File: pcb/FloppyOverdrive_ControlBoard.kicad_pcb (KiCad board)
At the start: 2 copper layers, 163 x 104 mm, 0 parts

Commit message: PCB Update
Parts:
- added C1: 0.1u, Capacitor_THT:C_Disc_D5.0mm_W2.5mm_P2.50mm, F.Cu at (206.0, 97.0)
- added C2: 0.1u, Capacitor_THT:C_Disc_D5.0mm_W2.5mm_P2.50mm, F.Cu at (211.0, 97.0)
- added C3: 33u, Capacitor_THT:CP_Radial_D5.0mm_P2.00mm, F.Cu at (208.5, 65.0)
- added C4: 33u, Capacitor_THT:CP_Radial_D5.0mm_P2.00mm, F.Cu at (208.4, 57.0)
- added C5: 0.1u, Capacitor_THT:C_Disc_D5.0mm_W2.5mm_P2.50mm, F.Cu at (206.0, 91.0)
- added C6: 0.1u, Capacitor_THT:C_Disc_D5.0mm_W2.5mm_P2.50mm, F.Cu at (211.0, 91.0)
- added C7: 0.1u, Capacitor_THT:C_Disc_D5.0mm_W2.5mm_P2.50mm, F.Cu at (121.1, 42.0)
- added D1: LED1, LED_THT:LED_D5.0mm, F.Cu at (170.0, 98.0)
- added D2: LED2, LED_THT:LED_D5.0mm, F.Cu at (177.0, 98.0)
- added D3: LED3, LED_THT:LED_D5.0mm, F.Cu at (184.0, 98.0)
- added D4: LED4, LED_THT:LED_D5.0mm, F.Cu at (191.0, 98.0)
- added FB1: FerriteBead, Resistor_SMD:R_1206_3216Metric, F.Cu at (209.0, 71.0)
- added FB2: FerriteBead, Resistor_SMD:R_1206_3216Metric, F.Cu at (209.0, 50.3)
- added J1: 174804-1, 174804-1:1748041, F.Cu at (216.2, 53.4)
- added J2: Motor_Header, 440055-4:SHDRRA4W50P15X200_1X4_1000X770X525P, F.Cu at (194.2, 134.4)
- added J3: Bus_Connector, Connector_PinHeader_2.54mm:PinHeader_2x17_P2.54mm_Horizontal, F.Cu at (212.0, 102.0)
- added J4: Sensor_Header, Connector_PinHeader_2.54mm:PinHeader_2x05_P2.54mm_Horizontal, F.Cu at (78.7, 142.1)
- added J5: Heads_Header, Connector_PinHeader_2.54mm:PinHeader_2x05_P2.54mm_Horizontal, F.Cu at (78.7, 114.1)
- added J6: Step_Header, Connector_PinHeader_2.00mm:PinHeader_2x05_P2.00mm_Horizontal, F.Cu at (187.0, 134.9)
- added J7: PIC_ADC_Header, Connector_PinHeader_2.54mm:PinHeader_2x02_P2.54mm_Vertical, F.Cu at (144.0, 23.4)
- added J8: FPGA_IO_Header, Connector_PinHeader_2.54mm:PinHeader_2x20_P2.54mm_Vertical, F.Cu at (115.0, 143.0)
- added J9: HeadOut_Header, Connector_PinHeader_2.54mm:PinHeader_2x04_P2.54mm_Vertical, F.Cu at (93.3, 112.8)
- added JP1: LED_Enable, Connector_PinHeader_2.54mm:PinHeader_1x02_P2.54mm_Vertical, F.Cu at (199.0, 97.0)
- added R1: 220, Resistor_THT:R_Axial_DIN0207_L6.3mm_D2.5mm_P10.16mm_Horizontal, F.Cu at (48.9, 82.0)
- added R10: 47k, Resistor_THT:R_Axial_DIN0207_L6.3mm_D2.5mm_P10.16mm_Horizontal, F.Cu at (59.8, 66.4)
- added R11: 1k, Resistor_THT:R_Axial_DIN0207_L6.3mm_D2.5mm_P10.16mm_Horizontal, F.Cu at (72.0, 62.3)
- added R12: 510, Resistor_THT:R_Axial_DIN0207_L6.3mm_D2.5mm_P10.16mm_Horizontal, F.Cu at (164.1, 95.0)
- added R13: 510, Resistor_THT:R_Axial_DIN0207_L6.3mm_D2.5mm_P10.16mm_Horizontal, F.Cu at (153.9, 98.0)
- added R14: 510, Resistor_THT:R_Axial_DIN0207_L6.3mm_D2.5mm_P10.16mm_Horizontal, F.Cu at (164.1, 101.0)
- added R15: 510, Resistor_THT:R_Axial_DIN0207_L6.3mm_D2.5mm_P10.16mm_Horizontal, F.Cu at (164.1, 104.0)
- added R2: 220, Resistor_THT:R_Axial_DIN0207_L6.3mm_D2.5mm_P10.16mm_Horizontal, F.Cu at (35.5, 82.0)
- added R3: 220, Resistor_THT:R_Axial_DIN0207_L6.3mm_D2.5mm_P10.16mm_Horizontal, F.Cu at (62.2, 82.6)
- added R4: 47k, Resistor_THT:R_Axial_DIN0207_L6.3mm_D2.5mm_P10.16mm_Horizontal, F.Cu at (59.8, 70.4)
- added R5: 10k, Resistor_THT:R_Axial_DIN0207_L6.3mm_D2.5mm_P10.16mm_Horizontal, F.Cu at (115.5, 37.9)
- added R6: 1k, Resistor_THT:R_Axial_DIN0207_L6.3mm_D2.5mm_P10.16mm_Horizontal, F.Cu at (73.1, 66.4)
- added R7: 1k, Resistor_THT:R_Axial_DIN0207_L6.3mm_D2.5mm_P10.16mm_Horizontal, F.Cu at (58.7, 62.3)
- added R8: 22k, Resistor_THT:R_Axial_DIN0207_L6.3mm_D2.5mm_P10.16mm_Horizontal, F.Cu at (73.1, 70.4)
- added R9: 220, Resistor_THT:R_Axial_DIN0207_L6.3mm_D2.5mm_P10.16mm_Horizontal, F.Cu at (62.2, 78.5)
- added SW1: RST_Btn, Button_Switch_THT:SW_PUSH_6mm, F.Cu at (138.2, 103.2)
- added U1: TXB0108-PW, Package_SO:TSSOP-20_4.4x6.5mm_P0.65mm, F.Cu at (197.0, 112.0)
- added U2: TXB0108-PW, Package_SO:TSSOP-20_4.4x6.5mm_P0.65mm, F.Cu at (197.0, 122.0)
- added U3: ULN2003, Package_SO:TSSOP-16_4.4x5mm_P0.65mm, F.Cu at (184.0, 128.0)
- added U4: IceWerx FPGA, IceWerx:IceWerx FPGA, F.Cu at (139.0, 123.0)

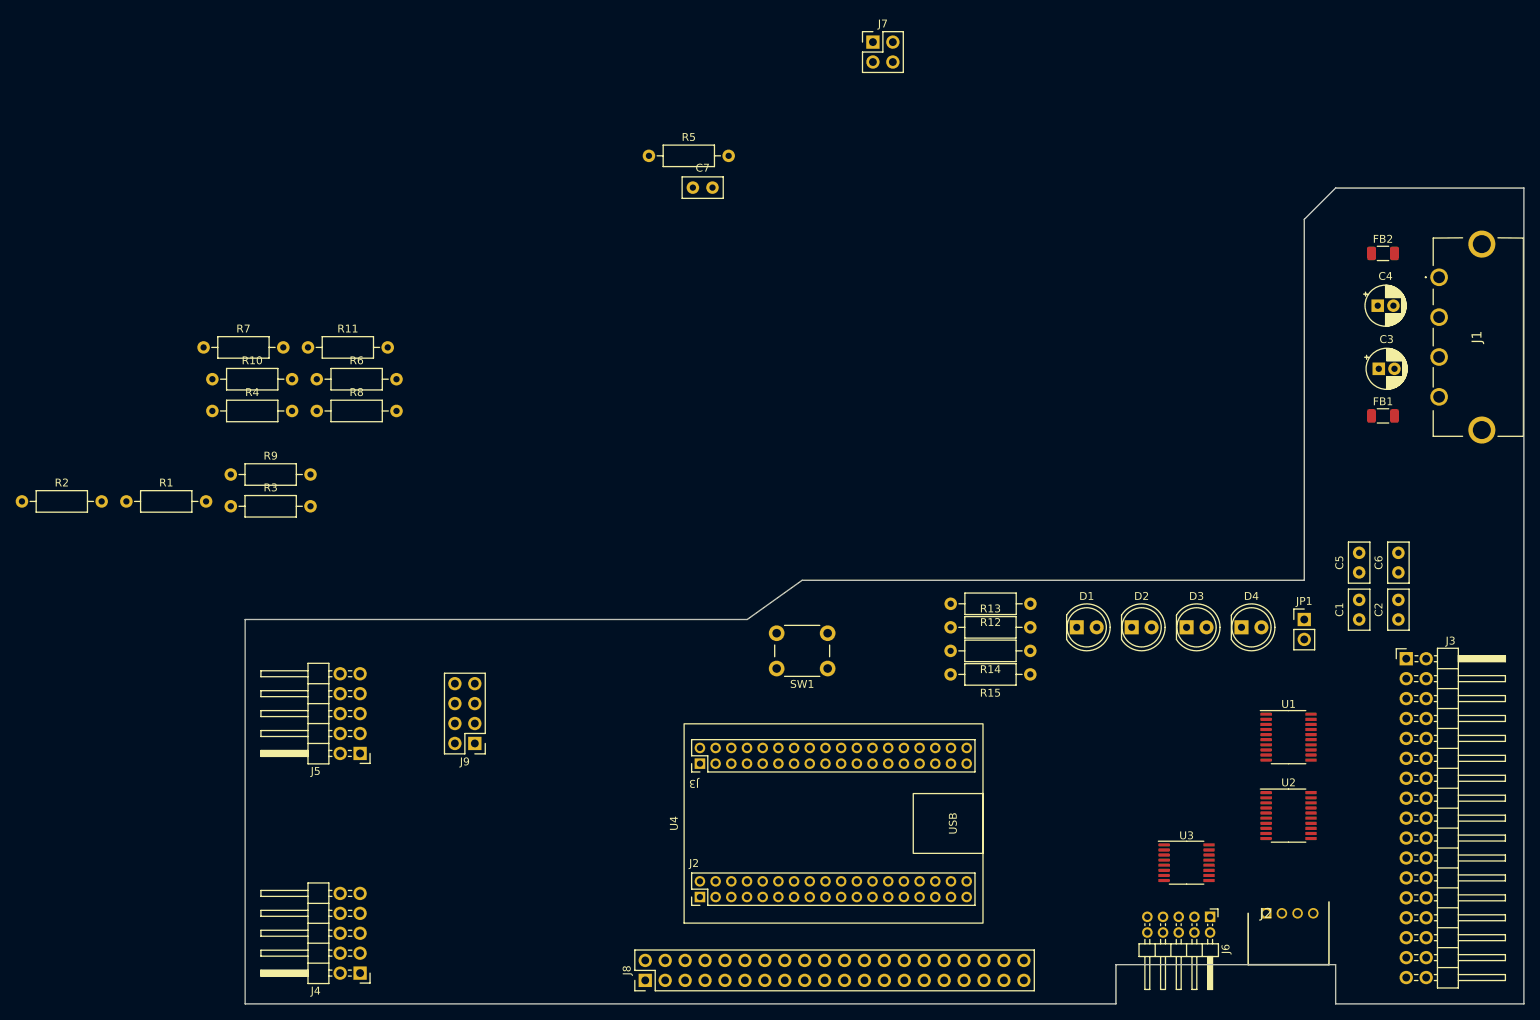
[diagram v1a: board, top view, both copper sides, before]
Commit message: Worked on PCB layout, began adding test points
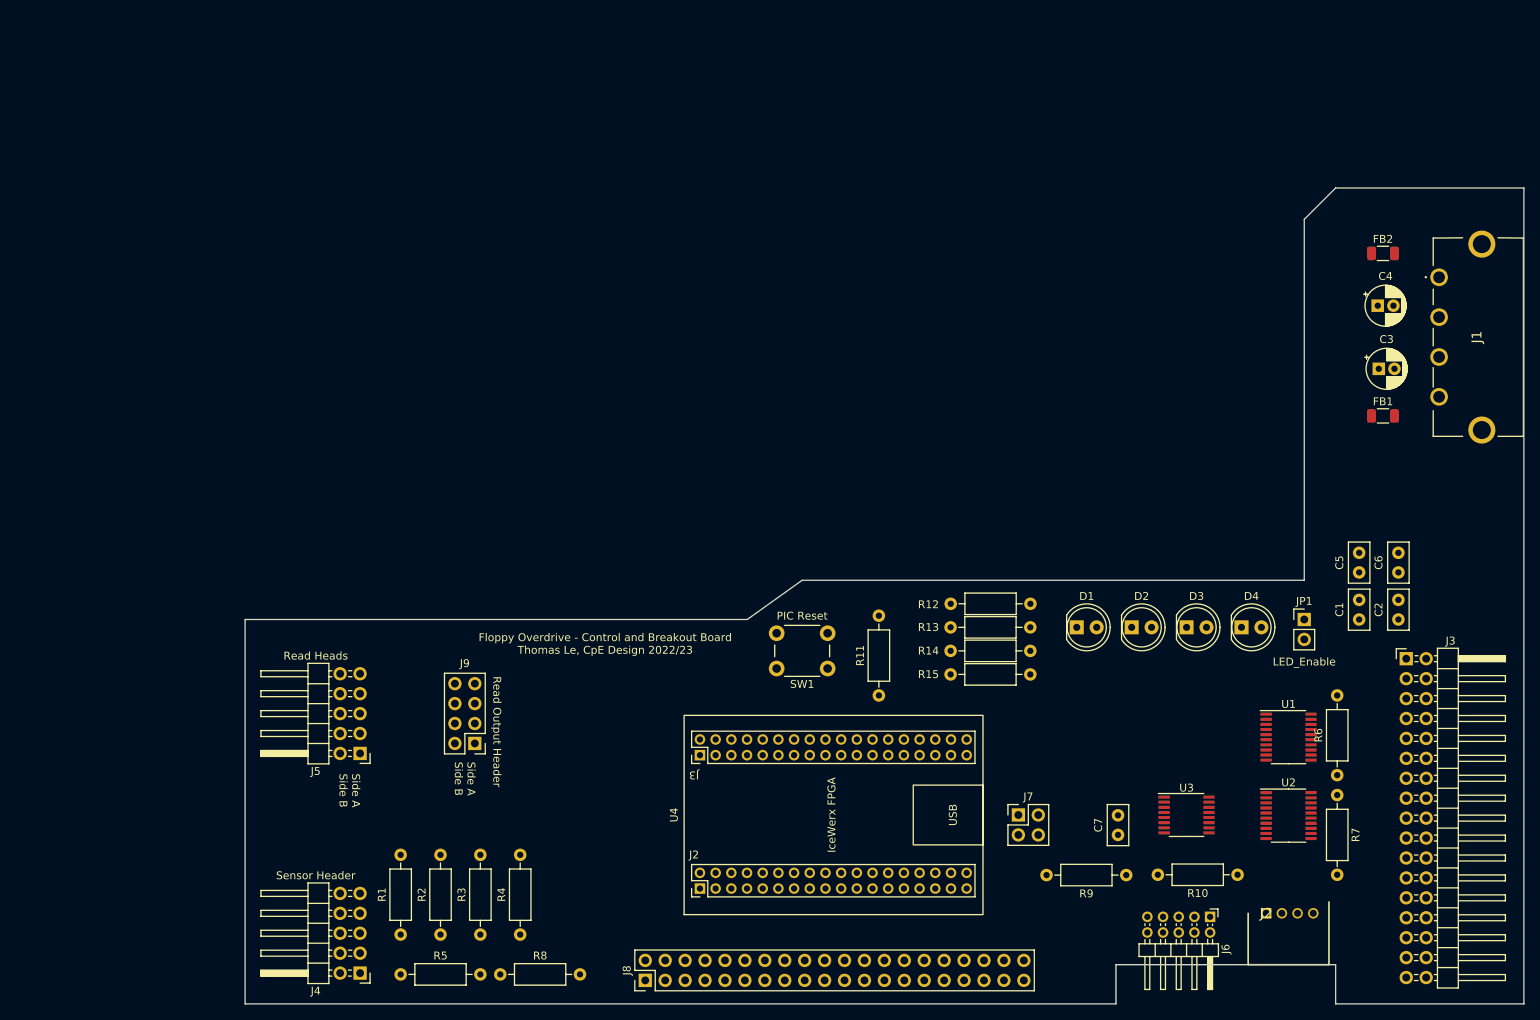
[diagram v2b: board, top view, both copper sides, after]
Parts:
- J4: value Sensor_Header -> Sensor Header
- J5: value Heads_Header -> Read Heads
- SW1: value RST_Btn -> PIC Reset
- moved R7 155.4 mm to (203.2, 119.4), turned to -90 degrees
- moved R10 145.1 mm to (190.5, 129.5), turned to 180 degrees
- moved R6 139.5 mm to (203.2, 116.8), turned to 90 degrees
- moved R9 125.0 mm to (176.3, 129.6), turned to 180 degrees
- moved R5 109.0 mm to (83.8, 142.2)
- moved J7 100.2 mm to (162.6, 121.9)
- moved C7 98.7 mm to (175.3, 124.5), turned to 90 degrees
- moved R11 85.2 mm to (144.8, 106.7), turned to 90 degrees
- moved R4 77.4 mm to (99.1, 137.2), turned to 90 degrees
- moved R2 76.8 mm to (88.9, 137.2), turned to 90 degrees
- moved R8 75.5 mm to (96.5, 142.2)
- moved R1 65.3 mm to (83.8, 137.2), turned to 90 degrees
- moved R3 63.2 mm to (94.0, 137.2), turned to 90 degrees
- moved U3 6.08 mm to (184.0, 121.9)
- moved U4 1.08 mm to (139.0, 121.9)
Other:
- board text added: "Floppy Overdrive - Control and Breakout Board Thomas Le, CpE Design 2022/23"
- board text added: "Read Output Header"
- board text added: "Side A Side B"

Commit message: Routing first draft
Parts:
- added TP1: TP_5V, TestPoint:TestPoint_Pad_D1.0mm, F.Cu at (202.0, 72.0)
- added TP2: TP_12V, TestPoint:TestPoint_Pad_D1.0mm, F.Cu at (202.0, 64.0)
- added TP3: TP_3V3, TestPoint:TestPoint_Pad_D1.0mm, F.Cu at (162.0, 121.0)
- J4: value Sensor Header -> Sensor_Header
- J5: value Read Heads -> Heads_Header
- SW1: value PIC Reset -> RST_Btn
- moved JP1 48.3 mm to (151.0, 102.0), turned to 180 degrees
- moved C7 15.5 mm to (163.0, 134.0)
- moved R9 12.2 mm to (170.0, 140.0), turned to 90 degrees
- moved J7 12.1 mm to (152.7, 129.0)
- moved U4 12.0 mm to (127.0, 123.0)
- moved R6 11.0 mm to (205.0, 106.0), turned to -90 degrees
- moved R15 9.79 mm to (167.8, 94.9), turned to -90 degrees
- moved R10 9.51 mm to (200.0, 130.0)
- moved J4 9.23 mm to (71.7, 136.1)
- moved R13 8.41 mm to (161.8, 94.9), turned to -90 degrees
- moved C3 7.11 mm to (207.0, 72.0)
- moved C4 7.11 mm to (206.9, 64.0)
- moved FB1 7.11 mm to (207.5, 78.0)
- moved FB2 7.11 mm to (207.5, 57.3)
- moved R14 6.12 mm to (164.8, 94.9), turned to -90 degrees
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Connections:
- J8 pad 17: Net-(J8-Pad17) -> Net-(U4-PadJ2.16)
- J8 pad 19: Net-(J8-Pad19) -> Net-(U4-PadJ2.17)
- J8 pad 21: Net-(J8-Pad21) -> Net-(U4-PadJ2.18)
- J8 pad 23: Net-(J8-Pad23) -> Net-(U4-PadJ2.19)
- J8 pad 25: Net-(J8-Pad25) -> Net-(U4-PadJ2.20)
- J8 pad 27: Net-(J8-Pad27) -> Net-(U4-PadJ2.21)
- J8 pad 29: Net-(J8-Pad29) -> Net-(U4-PadJ2.22)
- J8 pad 31: Net-(J8-Pad31) -> Net-(U4-PadJ2.23)
- J8 pad 33: Net-(J8-Pad33) -> Net-(U4-PadJ2.24)
- J8 pad 35: Net-(J8-Pad35) -> Net-(U4-PadJ2.25)
- J8 pad 37: Net-(J8-Pad37) -> Net-(U4-PadJ2.26)
- J8 pad 5: Net-(J8-Pad5) -> Net-(U4-PadJ2.9)
- R11 pad 2: +3.3V -> +3V3
- U4 pad J2.11: Net-(J8-Pad3) -> Net-(J8-Pad7)
- U4 pad J2.12: Net-(J8-Pad5) -> Net-(J8-Pad9)
- U4 pad J2.13: Net-(J8-Pad7) -> Net-(J8-Pad11)
- U4 pad J2.14: Net-(J8-Pad9) -> Net-(J8-Pad13)
- U4 pad J2.15: Net-(J8-Pad11) -> Net-(J8-Pad15)
- U4 pad J2.16: Net-(J8-Pad13) -> Net-(U4-PadJ2.16)
- U4 pad J2.17: Net-(J8-Pad15) -> Net-(U4-PadJ2.17)
- U4 pad J2.18: Net-(J8-Pad17) -> Net-(U4-PadJ2.18)
- U4 pad J2.19: Net-(J8-Pad19) -> Net-(U4-PadJ2.19)
- U4 pad J2.20: Net-(J8-Pad21) -> Net-(U4-PadJ2.20)
- U4 pad J2.21: Net-(J8-Pad23) -> Net-(U4-PadJ2.21)
- U4 pad J2.22: Net-(J8-Pad25) -> Net-(U4-PadJ2.22)
- U4 pad J2.23: Net-(J8-Pad27) -> Net-(U4-PadJ2.23)
- U4 pad J2.24: Net-(J8-Pad29) -> Net-(U4-PadJ2.24)
- U4 pad J2.25: Net-(J8-Pad31) -> Net-(U4-PadJ2.25)
- U4 pad J2.26: Net-(J8-Pad33) -> Net-(U4-PadJ2.26)
- U4 pad J2.27: Net-(J8-Pad35) -> PIN_38
- U4 pad J2.29: Net-(J8-Pad37) -> Motor_Control
- U4 pad J2.31: PIN_2 -> Speed_Control
- U4 pad J2.34: +3.3V -> +3V3
- U4 pad J2.7: Motor_Control -> Net-(J8-Pad3)
- U4 pad J2.9: Speed_Control -> Net-(U4-PadJ2.9)
- U4 pad J3.1: Density -> PIN_2
- U4 pad J3.10: WriteData -> PIN_20
- U4 pad J3.11: WriteGate -> PIN_22
- U4 pad J3.12: Track0 -> PIN_24
- U4 pad J3.13: WriteProtect -> PIN_26
- U4 pad J3.14: ReadData -> PIN_28
- U4 pad J3.15: SideSel -> PIN_30
- U4 pad J3.16: Ready -> PIN_32
- U4 pad J3.17: PIN_4 -> PIN_34
- U4 pad J3.18: PIN_6 -> PIN_36
- U4 pad J3.19: PIN_8 -> Ready
- U4 pad J3.2: DriveSel_3 -> PIN_4
- U4 pad J3.20: PIN_10 -> Density
- U4 pad J3.21: PIN_12 -> SideSel
- U4 pad J3.22: PIN_14 -> DriveSel_3
- U4 pad J3.23: PIN_16 -> ReadData
- U4 pad J3.24: PIN_18 -> Index
- U4 pad J3.25: PIN_20 -> WriteProtect
- U4 pad J3.26: PIN_22 -> DriveSel_0
- U4 pad J3.27: PIN_24 -> Track0
- U4 pad J3.28: PIN_26 -> DriveSel_1
- U4 pad J3.29: PIN_28 -> WriteGate
- U4 pad J3.3: Index -> PIN_6
- U4 pad J3.30: PIN_30 -> DriveSel_2
- U4 pad J3.31: PIN_32 -> WriteData
- U4 pad J3.32: PIN_34 -> Motor
- U4 pad J3.33: PIN_36 -> Step
- U4 pad J3.34: PIN_38 -> StepDir
- U4 pad J3.4: DriveSel_0 -> PIN_8
- U4 pad J3.5: DriveSel_1 -> PIN_10
- U4 pad J3.6: DriveSel_2 -> PIN_12
- U4 pad J3.7: Motor -> PIN_14
- U4 pad J3.8: StepDir -> PIN_16
- U4 pad J3.9: Step -> PIN_18
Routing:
- net +5V: track 0.00 -> 228.2 mm, vias 0 -> 3
- net +12V: track 0.00 -> 164.2 mm, vias 0 -> 1
- net Track0_Sens: track 0.00 -> 83.4 mm
- net Coil_1: track 0.00 -> 74.3 mm
- net Coil_2: track 0.00 -> 72.0 mm
- net Ready: track 0.00 -> 69.9 mm
- net Coil_3: track 0.00 -> 69.8 mm
- net Density: track 0.00 -> 67.9 mm
- net SideSel: track 0.00 -> 67.6 mm
- net Coil_4: track 0.00 -> 67.5 mm
- net DriveSel_3: track 0.00 -> 66.1 mm
- net ReadData: track 0.00 -> 65.3 mm
- net Index: track 0.00 -> 64.0 mm
- net WriteProtect: track 0.00 -> 63.1 mm
- net Motor_Control: track 0.00 -> 62.3 mm
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- added copper zone on B.Cu, net +3V3
- added copper zone on F.Cu, net GND
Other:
- outline, holes or cut-outs redrawn
